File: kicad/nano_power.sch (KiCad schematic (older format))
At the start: 22 parts, among them U1 IMX6UL_BGA289

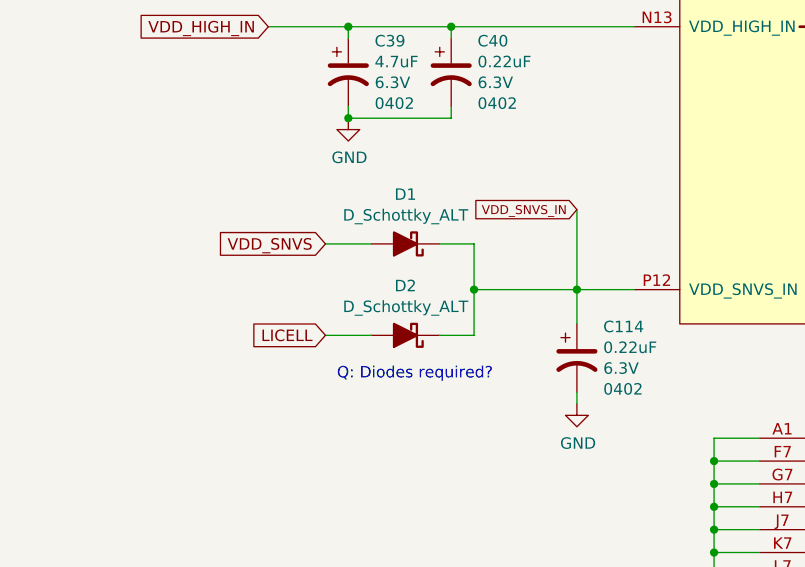
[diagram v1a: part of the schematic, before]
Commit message: remove vsnvs diodes
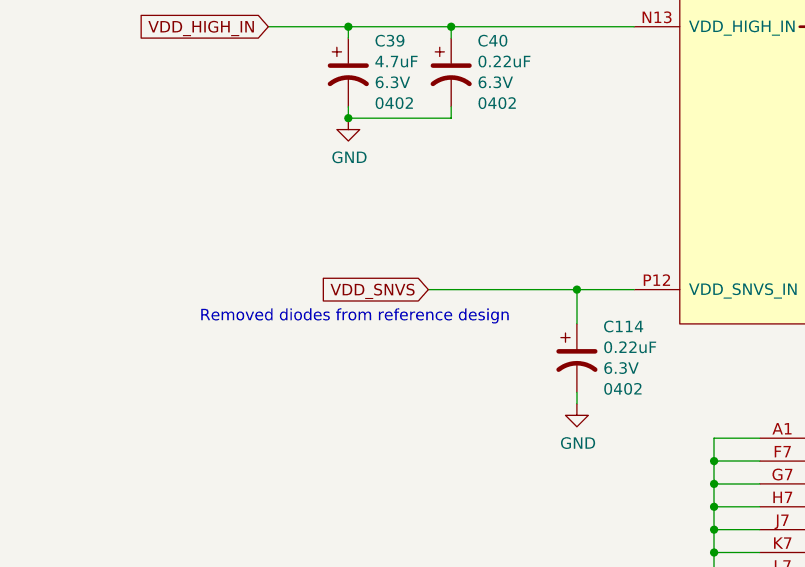
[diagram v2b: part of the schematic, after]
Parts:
- removed D1, D2: D_Schottky_ALT, Diode_SMD:D_0805_2012Metric, symbol Device:D_Schottky_ALT
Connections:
- net VDD_SNVS_IN is gone; now on net VDD_SNVS: C114.1, U1.P12 (VDD_SNVS_IN)
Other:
- note added: "Removed diodes from reference design"
- note removed: "Q: Diodes required?"
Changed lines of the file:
@@
 Text GLabel 2650 3000 0    50   Input ~ 0
 VDD_HIGH_IN
-Text GLabel 2900 3950 0    50   Input ~ 0
+Text GLabel 3350 4150 0    50   Input ~ 0
 VDD_SNVS
 Text GLabel 2200 1200 0    50   Input ~ 0
@@
 Wire Wire Line
 	7450 4500 7450 4550
-Text GLabel 2900 4350 0    50   Input ~ 0
-LICELL
-$Comp
-L Device:D_Schottky_ALT D1
-U 1 1 5C318A68
-P 3250 3950
-F 0 "D1" H 3250 3734 50  0000 C CNN
-F 1 "D_Schottky_ALT" H 3250 3825 50  0000 C CNN
-F 2 "Diode_SMD:D_0805_2012Metric" H 3250 3950 50  0001 C CNN
-F 3 "~" H 3250 3950 50  0001 C CNN
-	1    3250 3950
-	-1   0    0    1
-$EndComp
-$Comp
-L Device:D_Schottky_ALT D2
-U 1 1 5C318B1E
-P 3250 4350
-F 0 "D2" H 3250 4134 50  0000 C CNN
-F 1 "D_Schottky_ALT" H 3250 4225 50  0000 C CNN
-F 2 "Diode_SMD:D_0805_2012Metric" H 3250 4350 50  0001 C CNN
-F 3 "~" H 3250 4350 50  0001 C CNN
-	1    3250 4350
-	-1   0    0    1
-$EndComp
-Wire Wire Line
-	2900 3950 3100 3950
-Wire Wire Line
-	2900 4350 3100 4350
-Wire Wire Line
-	3400 3950 3550 3950
-Wire Wire Line
-	3550 3950 3550 4150
-Wire Wire Line
-	3550 4350 3400 4350
-Connection ~ 3550 4150
-Wire Wire Line
-	3550 4150 3550 4350
-Wire Wire Line
-	3550 4150 4000 4150
-Text Notes 2950 4550 0    50   ~ 0
-Q: Diodes required?
+Text Notes 2350 4300 0    50   ~ 0
+Removed diodes from reference design
 Wire Wire Line
 	7850 2300 7850 2400
@@
 Wire Wire Line
 	2650 3000 3000 3000
-Text GLabel 4000 3800 0    39   Input ~ 0
-VDD_SNVS_IN
-Wire Wire Line
-	4000 3800 4000 4150
+Wire Wire Line
+	3350 4150 4000 4150
 $EndSCHEMATC
